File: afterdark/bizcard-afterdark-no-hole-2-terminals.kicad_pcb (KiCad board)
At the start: 2 copper layers, 35.9 x 20.8 mm, 4 parts

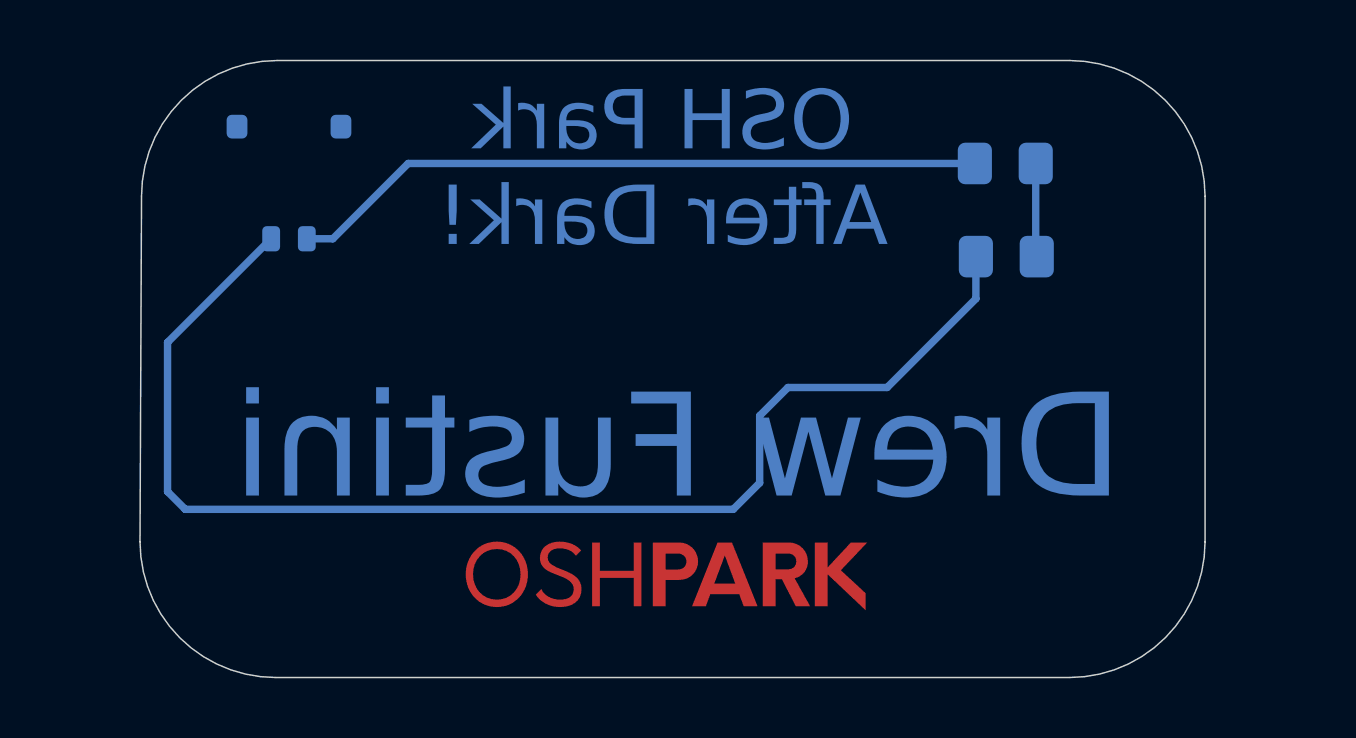
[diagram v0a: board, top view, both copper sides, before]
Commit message: make After Dark with no hole and SMD pads for power
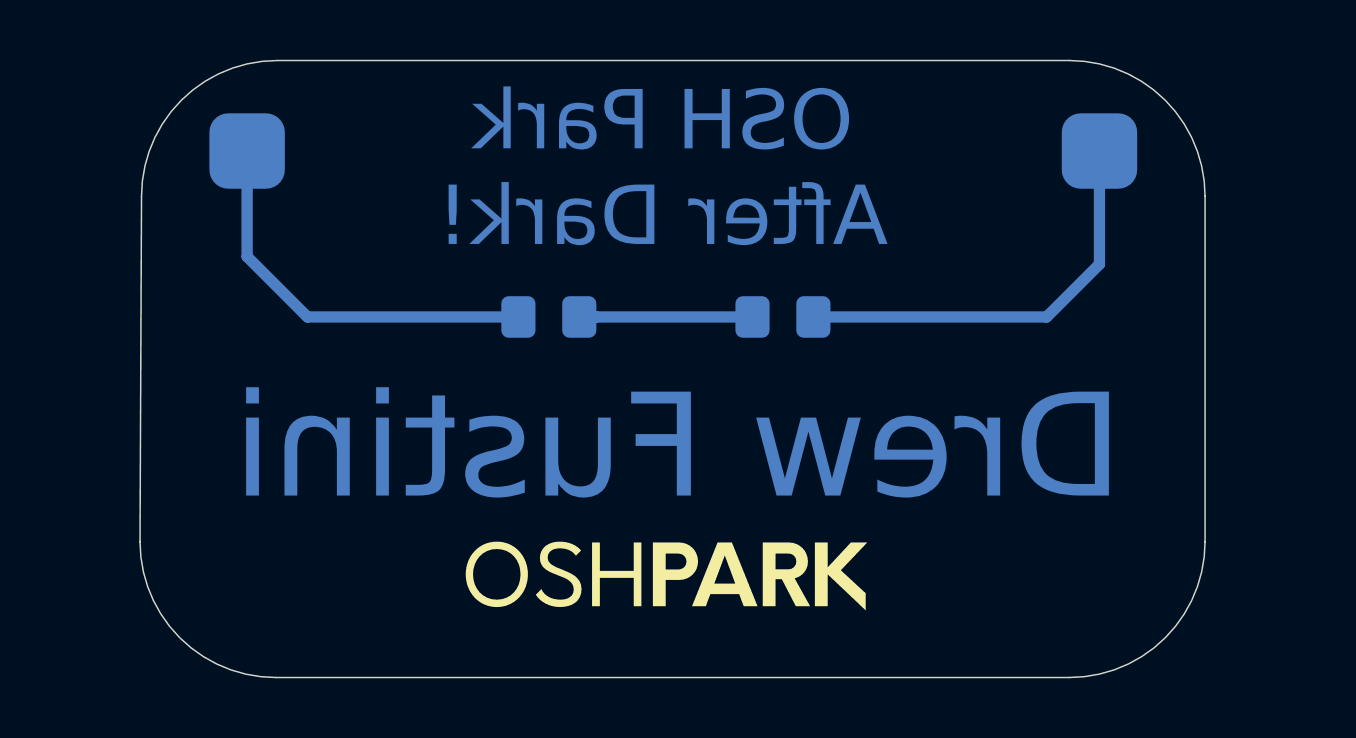
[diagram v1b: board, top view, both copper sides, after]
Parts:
- removed the REF** at (131.7, 65.8)
- added REF**: PinHeader_1x01_P2.54mm_Vertical, afterdark:PinHeader_1x01_P2.54mm_Vertical, F.Cu at (130.3, 64.8)
- added REF**: PinHeader_1x01_P2.54mm_Vertical, afterdark:PinHeader_1x01_P2.54mm_Vertical, B.Cu at (159.0, 64.8)
- moved REF** 16.2 mm to (140.5, 70.4)
- moved REF** 7.79 mm to (148.3, 70.4)
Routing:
- net (no net): track 69.8 -> 33.5 mm
